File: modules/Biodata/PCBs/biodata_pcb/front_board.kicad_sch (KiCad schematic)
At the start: 20 parts, among them J1 THONKICONN, J2 THONKICONN, J3 THONKICONN, J4 THONKICONN, J5 THONKICONN, J6 THONKICONN, J7 THONKICONN, J8 THONKICONN

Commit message: v0.1 biodata pcb
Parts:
- added D3: LED, LED_THT:LED_D5.0mm, symbol Device:LED
- added J10, J12, J8, J9: THONKICONN, FreeModular:THONKICONN, symbol FreeModular:THONKICONN
- added R16, R17: 1kΩ, Resistor_THT:R_Axial_DIN0207_L6.3mm_D2.5mm_P10.16mm_Horizontal, symbol Device:R
- added RV7, RV8: 50kΩ, Potentiometer_THT:Potentiometer_Alpha_RD901F-40-00D_Single_Vertical, symbol Device:R_Potentiometer
- D1: renamed from D2; footprint (none) -> LED_THT:LED_D5.0mm
- D2: renamed from D1; footprint (none) -> LED_THT:LED_D5.0mm
- RV1, RV2, RV3, RV4, RV5, RV6: footprint (none) -> Potentiometer_THT:Potentiometer_Alpha_RD901F-40-00D_Single_Vertical
- renumbered J8 to J11, J7 to J2, J2 to J3, J3 to J4, J4 to J5, J5 to J6, J6 to J7, R13 to R11, R11 to R12, R12 to R13
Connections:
- net +5V: now also RV7.1, RV8.1
- net GND: now also D3.1 (K), J10.1, J12.1, J8.1, J9.1, RV7.3, RV8.3
- net cv_out_a: now also J4.3; no longer R12.2, R13.2
- net cv_out_b: now also J7.3; no longer R10.2, R11.2
- net gate_out_a: now also R10.2, R11.2; no longer J4.3
- net gate_out_b: now also R12.2, R13.2; no longer J7.3
- net raw_out: now also J12.3; no longer J11.3
- net slew_a: now also RV4.2; no longer RV3.2
- net slew_b: now also RV6.2; no longer RV5.2
- net spread_a: now also RV3.2; no longer RV4.2
- net spread_b: now also RV5.2; no longer RV6.2
- new net: J8.3, R16.1
- new net: D3.2 (A), R17.1
- new net cv_out: J11.3
- new net cv_out_c: J10.3
- new net gate_in_c: J9.3
- new net gate_out_c: R16.2, R17.2
- new net slew_c: RV8.2
- new net spread_c: RV7.2
- no-connect marks 8 -> 12
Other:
- company: (none) -> Free Modular
- title: (none) -> Biodata
- moved on the sheet: D1, D2, J1, J11, J2, J3, J4, J5, J6, J7, R10, R11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

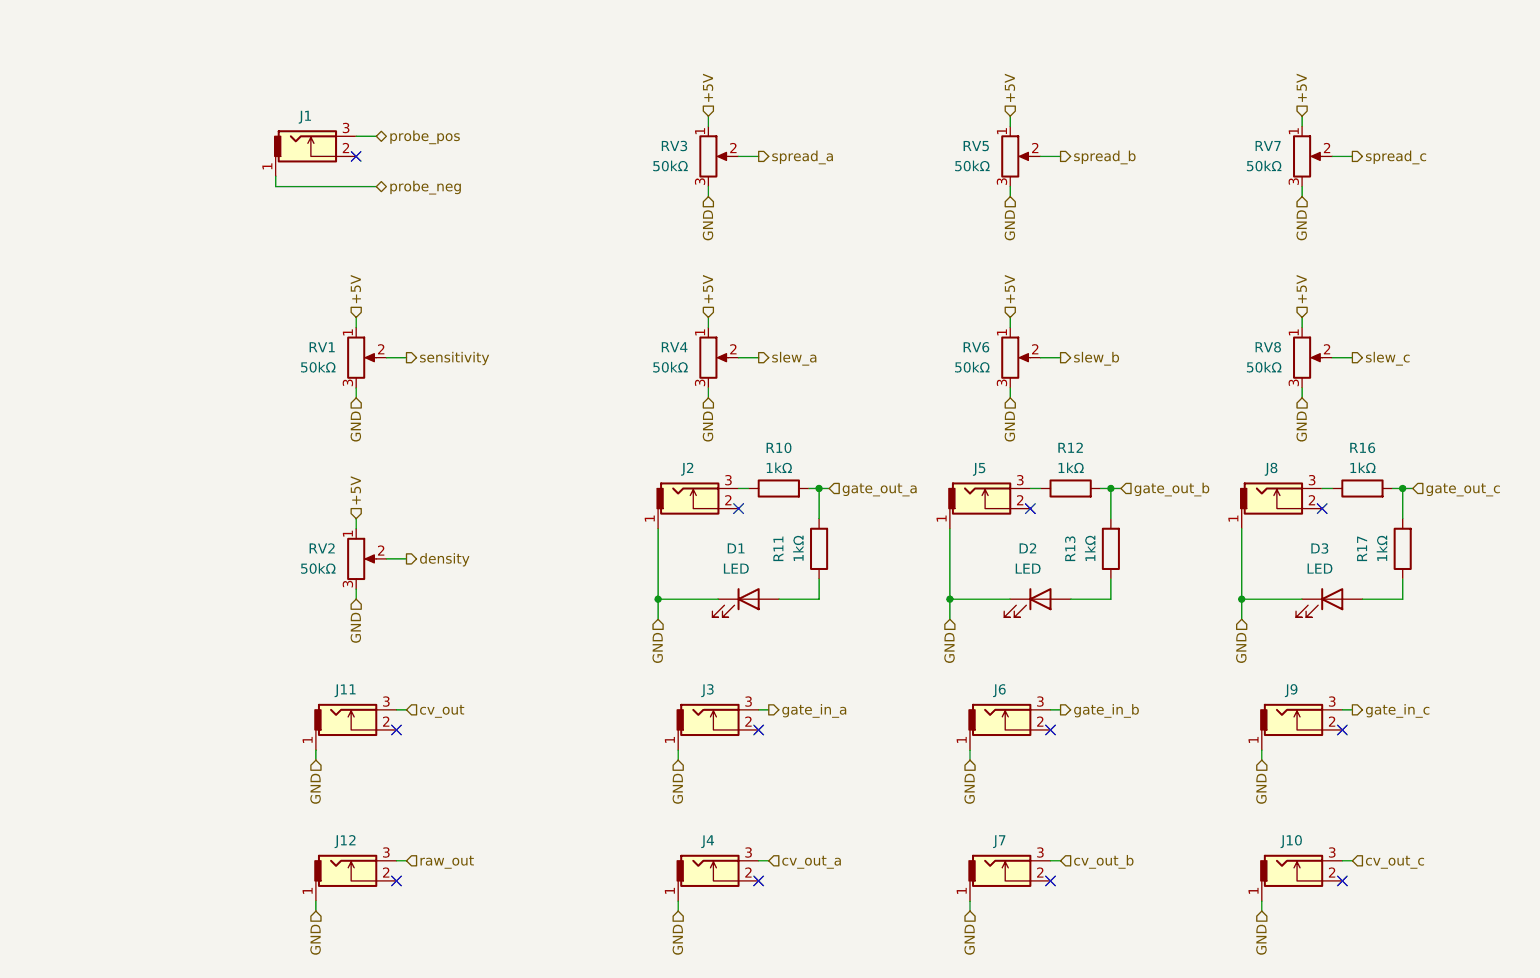
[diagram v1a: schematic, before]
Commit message: Switch biodata to monophonic
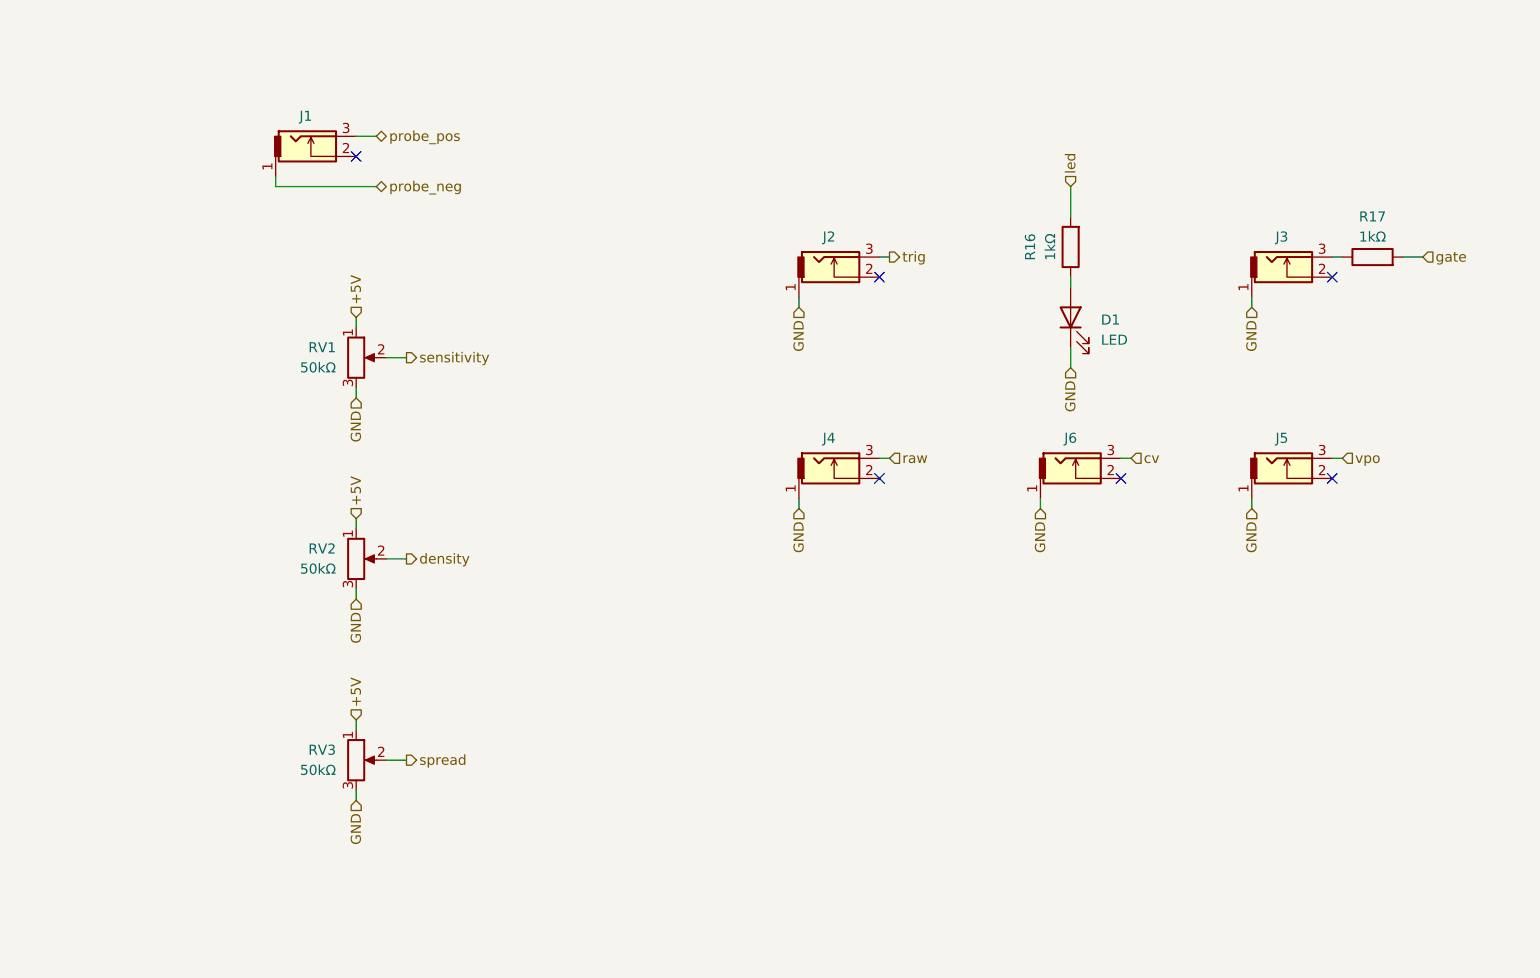
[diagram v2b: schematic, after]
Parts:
- removed D2, D3: LED, LED_THT:LED_D5.0mm, symbol Device:LED
- removed J10, J5, J6, J7, J8, J9: THONKICONN, FreeModular:THONKICONN, symbol FreeModular:THONKICONN
- removed R12, R13, R16, R17: 1kΩ, Resistor_THT:R_Axial_DIN0207_L6.3mm_D2.5mm_P10.16mm_Horizontal, symbol Device:R
- removed RV4, RV5, RV6, RV7, RV8: 50kΩ, Potentiometer_THT:Potentiometer_Alpha_RD901F-40-00D_Single_Vertical, symbol Device:R_Potentiometer
- RV2, RV3: footprint Potentiometer_THT:Potentiometer_Alpha_RD901F-40-00D_Single_Vertical -> FreeModular:Potentiometer_Alpha_Single_Vertical_trim
- renumbered J3 to J2, J2 to J3, J12 to J4, J4 to J5, J11 to J6, R11 to R16, R10 to R17
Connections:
- net cv_out renamed cv
- net cv_out_a renamed vpo
- net gate_in_a renamed trig
- net gate_out_a renamed gate
- net gate: no longer R16.2
- net raw_out renamed raw
- net spread_a renamed spread
- new net led: R16.2
- no-connect marks 12 -> 6
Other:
- moved on the sheet: D1, J2, J3, J4, J5, J6, R16, R17, RV3

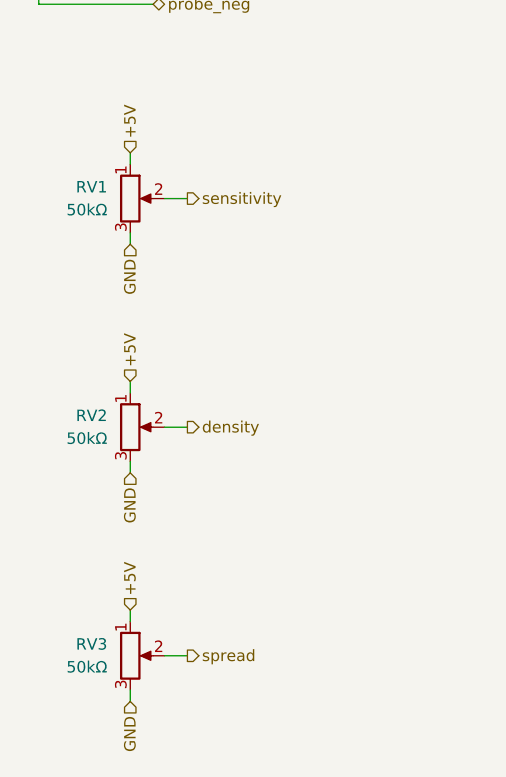
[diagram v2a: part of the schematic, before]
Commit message: Rearrange biodata PCB to allow mounting bolt; update CV algorithm
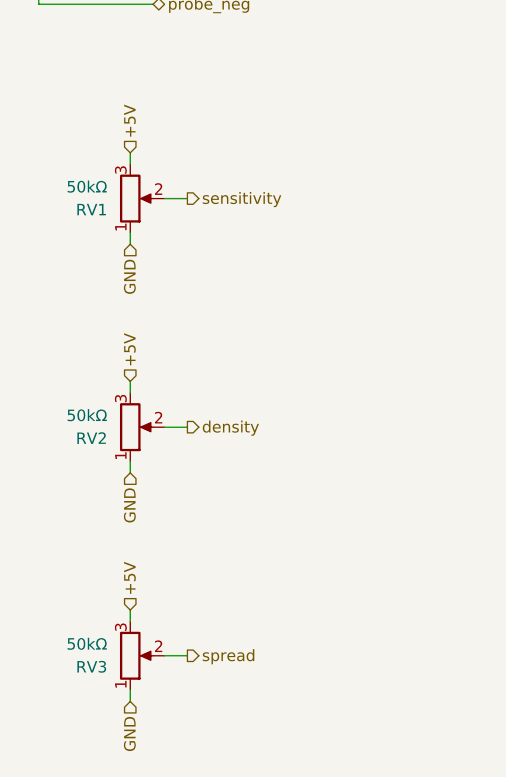
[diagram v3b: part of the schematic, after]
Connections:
- net +5V: now also RV1.3, RV2.3, RV3.3; no longer RV1.1, RV2.1, RV3.1
- net GND: now also RV1.1, RV2.1, RV3.1; no longer RV1.3, RV2.3, RV3.3
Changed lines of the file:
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@@
 		(lib_id "Device:R_Potentiometer")
 		(at 93.98 127 0)
-		(unit 1)
-		(exclude_from_sim no)
-		(in_bom yes)
-		(on_board yes)
-		(dnp no)
-		(fields_autoplaced yes)
+		(mirror x)
+		(unit 1)
+		(exclude_from_sim no)
+		(in_bom yes)
+		(on_board yes)
+		(dnp no)
 		(property "Reference" "RV3"
-			(at 91.44 125.7299 0)
+			(at 91.44 128.2701 0)
 			(effects
 				(font
@@
 		)
 		(property "Value" "50kΩ"
-			(at 91.44 128.2699 0)
+			(at 91.44 125.7301 0)
 			(effects
 				(font
@@
 		(lib_id "Device:R_Potentiometer")
 		(at 93.98 101.6 0)
-		(unit 1)
-		(exclude_from_sim no)
-		(in_bom yes)
-		(on_board yes)
-		(dnp no)
-		(fields_autoplaced yes)
+		(mirror x)
+		(unit 1)
+		(exclude_from_sim no)
+		(in_bom yes)
+		(on_board yes)
+		(dnp no)
 		(property "Reference" "RV2"
-			(at 91.44 100.3299 0)
+			(at 91.44 102.8701 0)
 			(effects
 				(font
@@
 		)
 		(property "Value" "50kΩ"
-			(at 91.44 102.8699 0)
+			(at 91.44 100.3301 0)
 			(effects
 				(font
@@
 		(lib_id "Device:R_Potentiometer")
 		(at 93.98 76.2 0)
-		(unit 1)
-		(exclude_from_sim no)
-		(in_bom yes)
-		(on_board yes)
-		(dnp no)
-		(fields_autoplaced yes)
+		(mirror x)
+		(unit 1)
+		(exclude_from_sim no)
+		(in_bom yes)
+		(on_board yes)
+		(dnp no)
 		(property "Reference" "RV1"
-			(at 91.44 74.9299 0)
+			(at 91.44 77.4701 0)
 			(effects
 				(font
@@
 		)
 		(property "Value" "50kΩ"
-			(at 91.44 77.4699 0)
-			(effects
-				(font
+			(at 91.44 74.9301 0)
+			(effects
+				(font
